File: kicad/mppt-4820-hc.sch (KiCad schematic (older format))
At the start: 18 parts, among them J1 MKDS 5/ 2-9,5, J2 MKDS 5/ 2-9,5, J3 MKDS 5/ 2-9,5, J4 8P8C, J5 8P8C, J6 JST PH

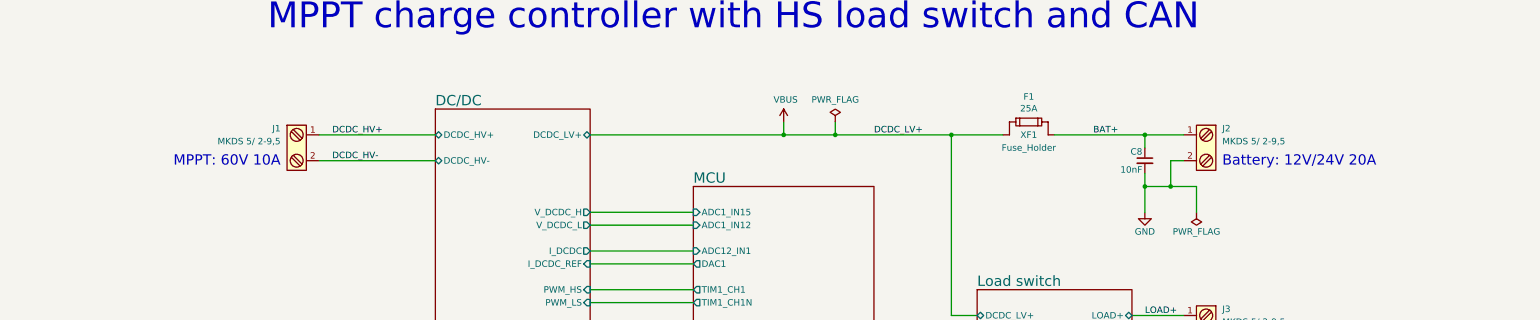
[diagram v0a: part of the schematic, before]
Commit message: Implement 1kW hardware upgrade: update component values in KiCad schematics and firmware constants
Co-authored-by: intrinsicaly <43327040+intrinsicaly@users.noreply.github.com>
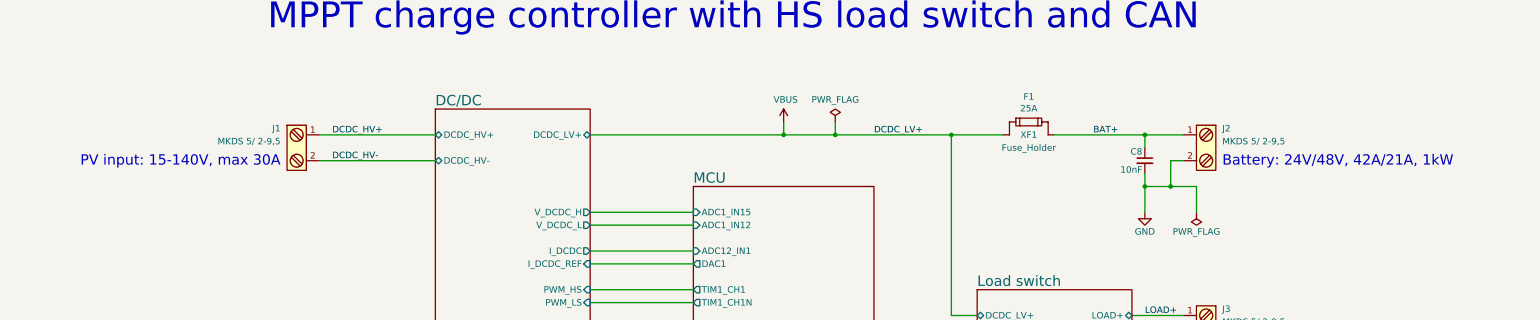
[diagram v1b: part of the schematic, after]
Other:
- note added: "Battery: 24V/48V, 42A/21A, 1kW"
- note added: "PV input: 15-140V, max 30A"
- note removed: "Battery: 12V/24V 20A"
- note removed: "MPPT: 60V 10A"
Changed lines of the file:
@@
 Title "MPPT 4820 HC"
 Date "2021-01-06"
-Rev "0.2.3"
+Rev "2.0"
 Comp "Copyright © 2020 Libre Solar Technologies GmbH"
 Comment1 "Licensed under CERN-OHL-W version 2"
@@
 PWR_INFO
 Text Notes 2000 2150 2    80   ~ 0
-MPPT: 60V 10A
+PV input: 15-140V, max 30A
 Text Notes 9300 2150 0    80   ~ 0
-Battery: 12V/24V 20A
+Battery: 24V/48V, 42A/21A, 1kW
 Text Notes 9300 3550 0    80   ~ 0
 Load output: 20A
